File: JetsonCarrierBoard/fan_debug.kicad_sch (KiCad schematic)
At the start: 13 parts

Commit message: Connections
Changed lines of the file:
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@@
     )
   )
-  (global_label "UART2_RXD" (shape input) (at 111.76 123.19 180) (fields_autoplaced)
+  (global_label "UART2_RXD" (shape output) (at 111.76 123.19 180) (fields_autoplaced)
     (effects (font (size 1.27 1.27)) (justify right))
     (property "Intersheet References" "${INTERSHEET_REFS}" (id 0) (at 98.7636 123.1106 0)

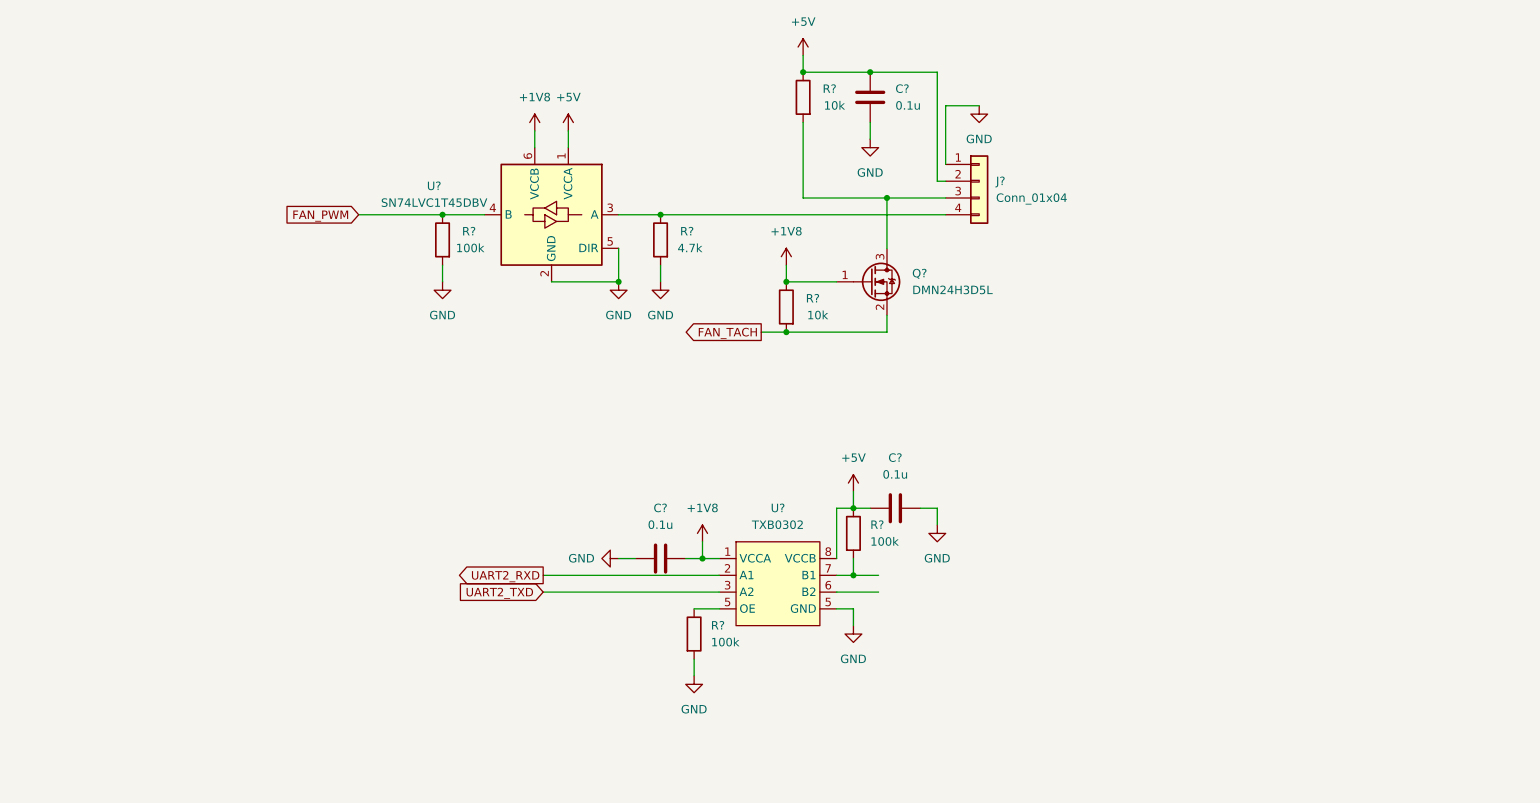
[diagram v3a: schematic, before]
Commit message: Button Header Pinout wiring
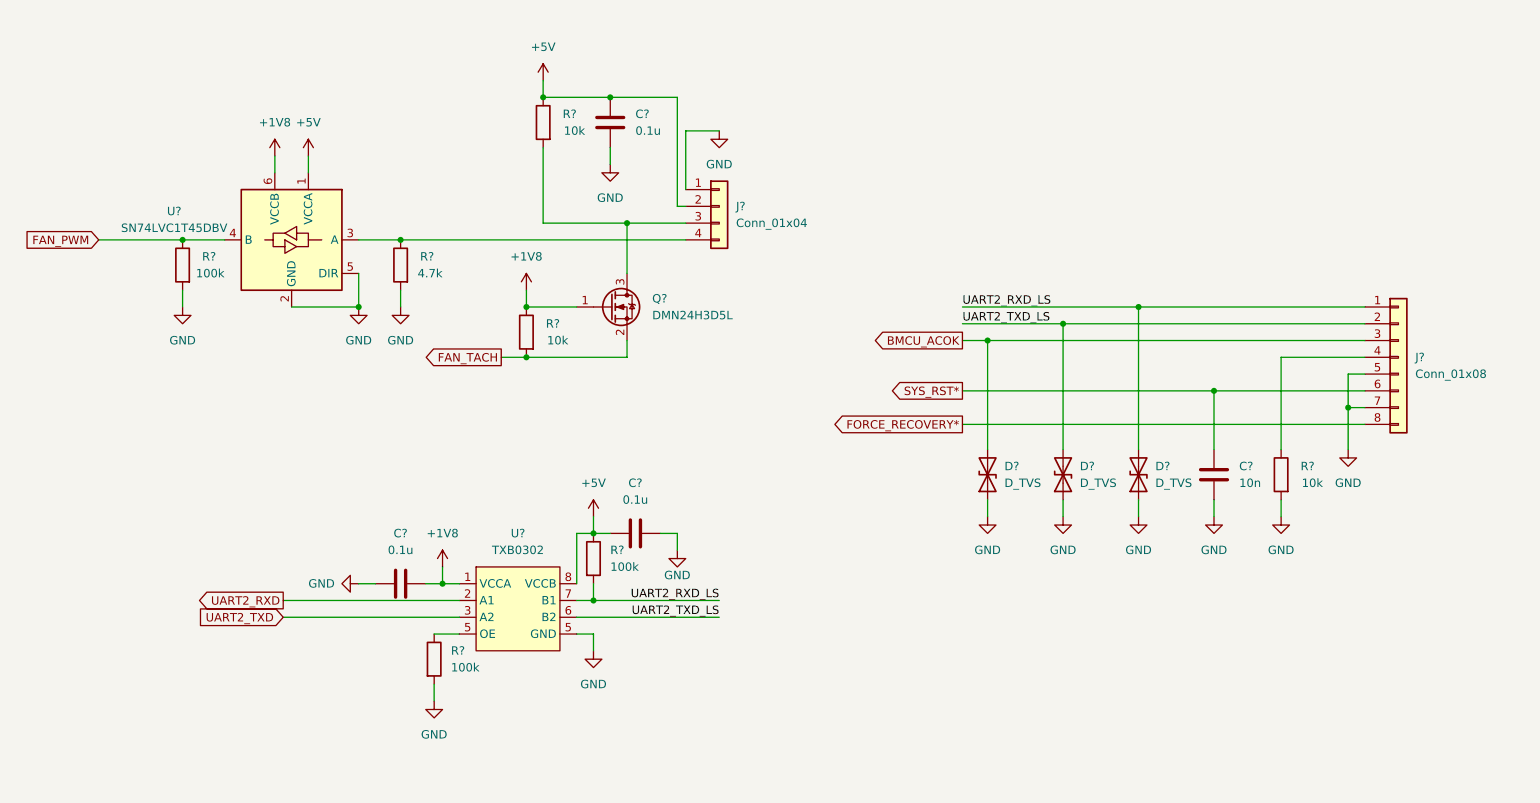
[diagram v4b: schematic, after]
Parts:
- added C?: 10n, symbol Device:C
- added D? (x3): D_TVS, symbol Device:D_TVS
- added J?: Conn_01x08, symbol Connector_Generic:Conn_01x08
- added R?: 10k, symbol Device:R
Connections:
- net GND: now also C?.2, D?.1 (A1), D?.1 (A1), D?.1 (A1), J?.5 (Pin_5), J?.7 (Pin_7), R?.2
- net UART2_TXD_LS: now reaches U?.6 (B2)
- net UART2_TXD_LS: now also D?.2 (A2), J?.2 (Pin_2)
- net UART2_RXD_LS: now reaches R?.2, U?.7 (B1)
- net UART2_RXD_LS: now also D?.2 (A2), J?.1 (Pin_1)
- new net: J?.4 (Pin_4), R?.1
- new net BMCU_ACOK: D?.2 (A2), J?.3 (Pin_3)
- new net FORCE_RECOVERY*: J?.8 (Pin_8)
- new net SYS_RST*: C?.1, J?.6 (Pin_6)
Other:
- moved on the sheet: C?, J?, Q?, R?, U?

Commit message: Added basic circuits, LED circuit, GPIO pins in GPIO page
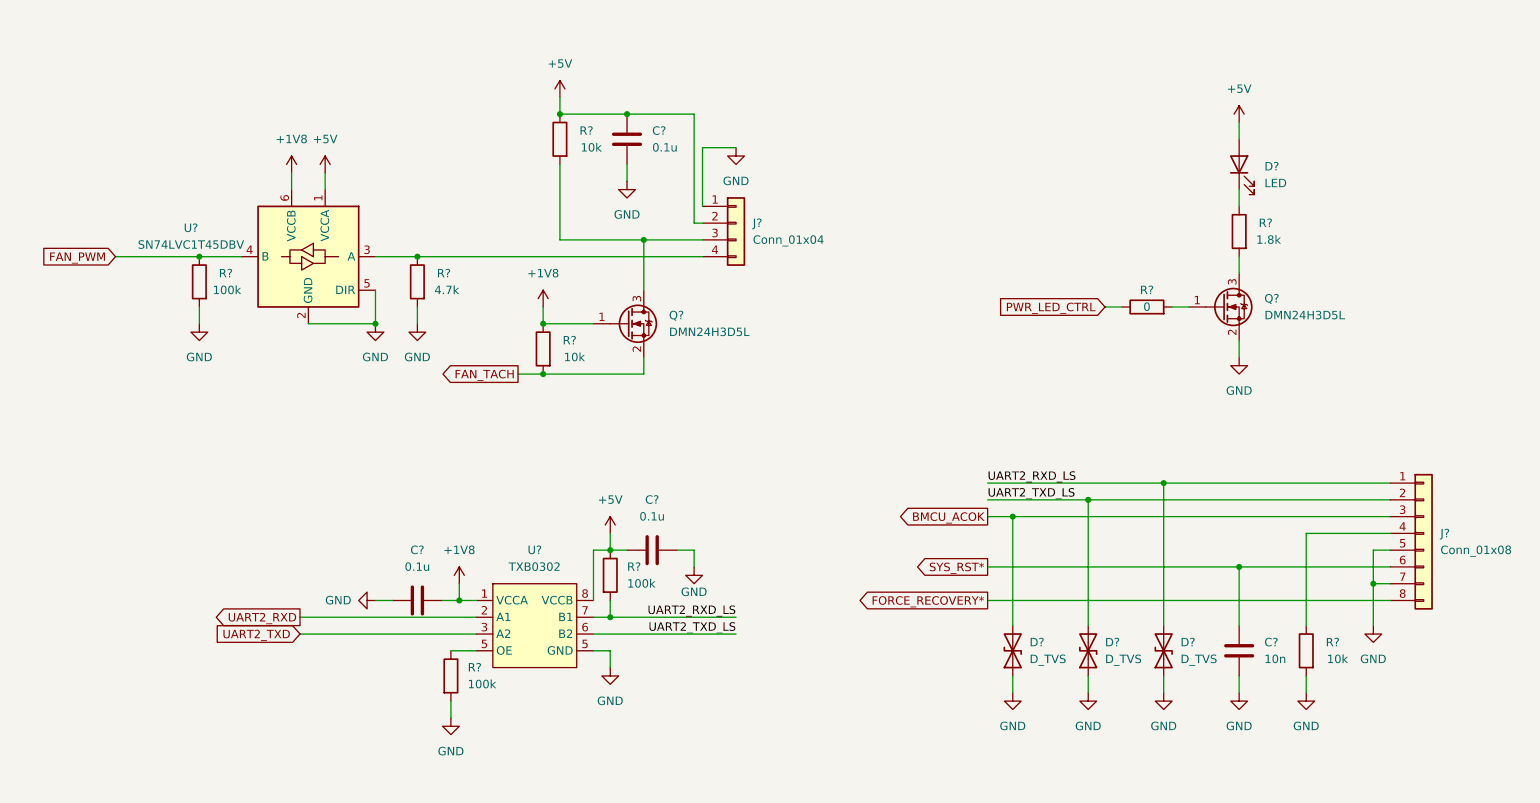
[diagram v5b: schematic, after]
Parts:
- added D?: LED, symbol Device:LED
- added Q?: DMN24H3D5L, Package_TO_SOT_SMD:SOT-23, symbol Transistor_FET:DMN24H3D5L
- added R?: 0, symbol Device:R
- added R?: 1.8k, symbol Device:R
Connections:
- net +5V: now also D?.2 (A)
- net GND: now also Q?.2 (S)
- new net: Q?.1 (G), R?.2
- new net: D?.1 (K), R?.1
- new net: Q?.3 (D), R?.2
- new net PWR_LED_CTRL: R?.1
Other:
- moved on the sheet: C?, D?, J?, Q?, R?, U?

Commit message: Adding more Title block info and changing main hierarchical page layout
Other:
- title: (none) -> Fan & Debug
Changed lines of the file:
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@@
 (kicad_sch (version 20211123) (generator eeschema)
   (paper "A4")
+  (title_block
+    (title "Fan & Debug")
+    (date "2022-09-18")
+    (rev "1.0")
+  )
   (junction (at 111.76 92.71) (diameter 0) (color 0 0 0 0)
   )

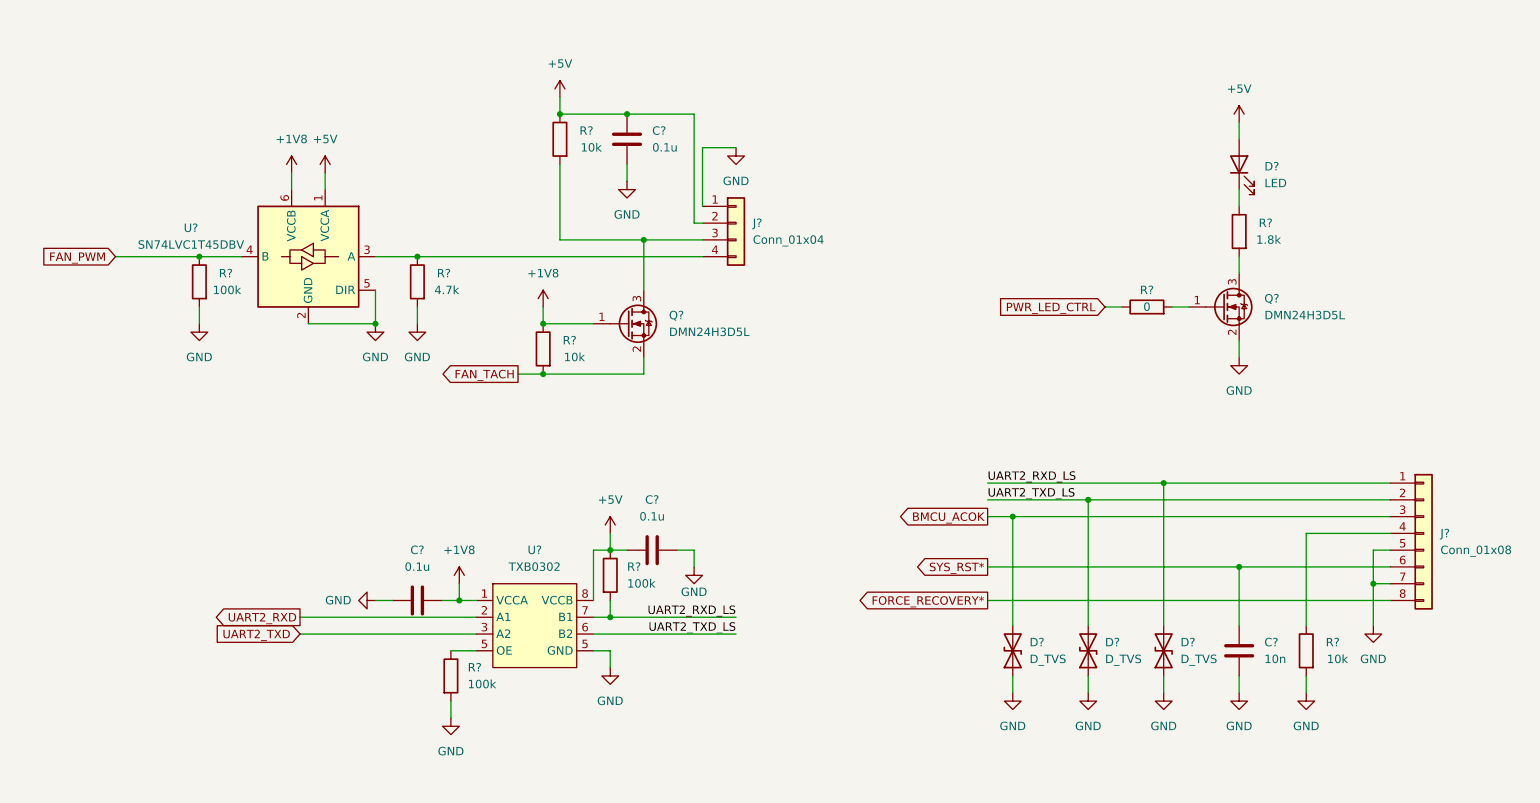
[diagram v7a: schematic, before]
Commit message: Improvement list, fixes, and readability improvements
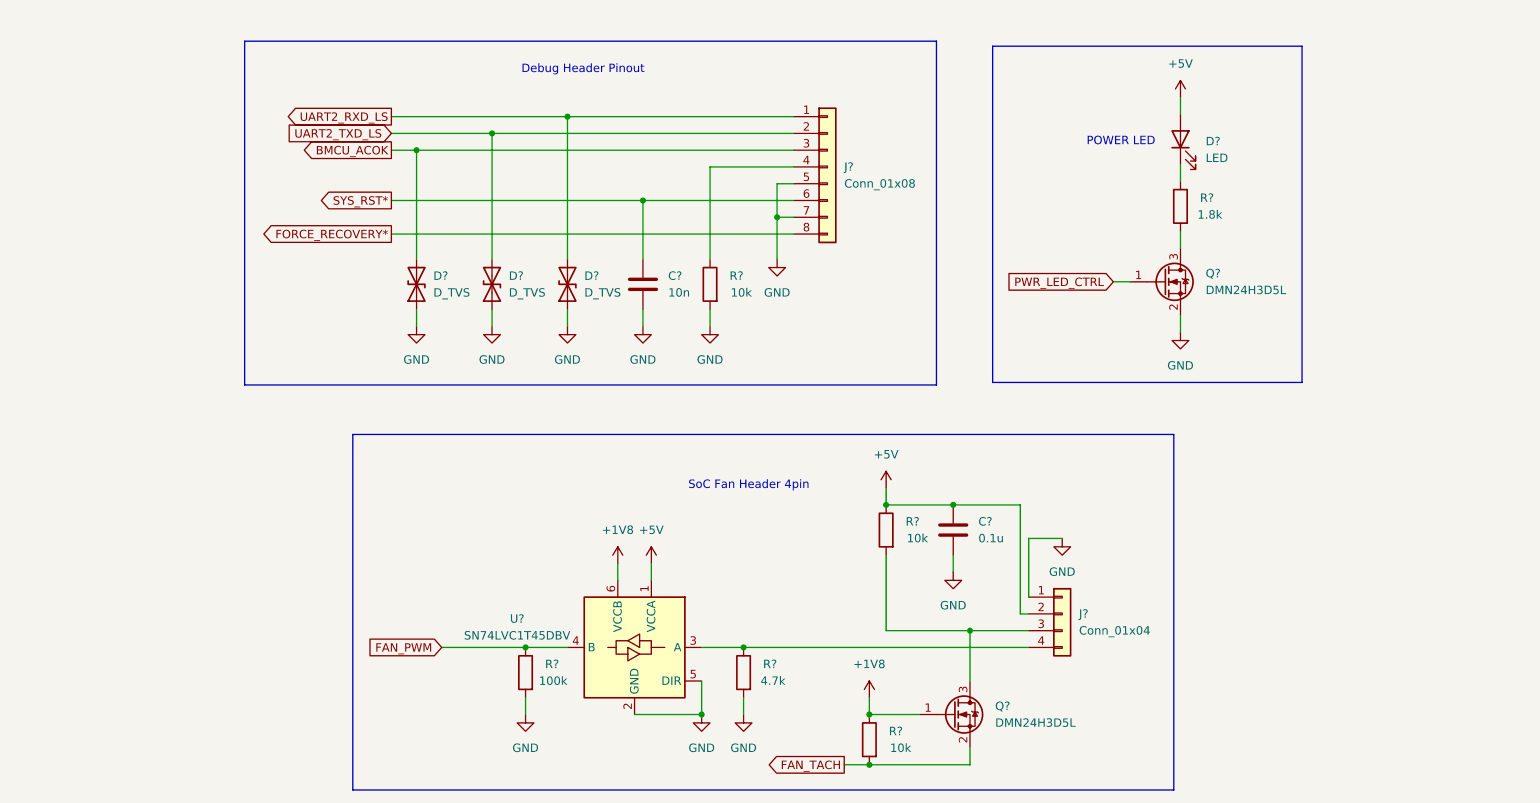
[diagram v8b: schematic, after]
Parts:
- removed C? (x2): 0.1u, symbol Device:C
- removed R?: 0, symbol Device:R
- removed R? (x2): 100k, symbol Device:R
- removed U?: TXB0302, symbol Logic_Level_Translator:TXB0302
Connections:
- net PWR_LED_CTRL: now also Q?.1 (G)
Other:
- note added: "Debug Header Pinout"
- note added: "POWER LED"
- note added: "SoC Fan Header 4pin"
- moved on the sheet: C?, D?, J?, Q?, R?, U?
